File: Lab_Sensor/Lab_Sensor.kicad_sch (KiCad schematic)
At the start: 31 parts, among them U1 ESP32-POE, U2 AM2302, U3 SSD1306, U4 INMP441

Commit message: switched pin 5 and 36
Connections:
- net at D6.A: now also R12.1
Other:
- moved on the sheet: D6
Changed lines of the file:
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@@
 	(wire
 		(pts
+			(xy 153.67 57.15) (xy 210.82 57.15)
+		)
+		(stroke
+			(width 0)
+			(type default)
+		)
+	)
+	(wire
+		(pts
 			(xy 87.63 62.23) (xy 90.17 62.23)
 		)
@@
 	(wire
 		(pts
-			(xy 59.69 90.17) (xy 59.69 92.71)
+			(xy 210.82 90.17) (xy 210.82 92.71)
 		)
 		(stroke
@@
 	(wire
 		(pts
+			(xy 210.82 57.15) (xy 210.82 82.55)
+		)
+		(stroke
+			(width 0)
+			(type default)
+		)
+	)
+	(wire
+		(pts
 			(xy 85.09 74.93) (xy 72.39 74.93)
 		)
@@
 	(symbol
 		(lib_id "Device:LED")
-		(at 59.69 86.36 90)
+		(at 210.82 86.36 90)
 		(unit 1)
 		(exclude_from_sim no)
@@
 		(dnp no)
 		(property "Reference" "D6"
-			(at 60.96 85.598 90)
+			(at 212.09 85.598 90)
 			(effects
 				(font
@@
 		)
 		(property "Value" "LED"
-			(at 60.96 87.63 90)
+			(at 212.09 87.63 90)
 			(effects
 				(font
@@
 		)
 		(property "Footprint" "Custom_Parts:Standard_LED_Throughhole"
-			(at 59.69 86.36 0)
+			(at 210.82 86.36 0)
 			(effects
 				(font
@@
 		)
 		(property "Datasheet" "~"
-			(at 59.69 86.36 0)
+			(at 210.82 86.36 0)
 			(effects
 				(font
@@
 		)
 		(property "Description" "Light emitting diode"
-			(at 59.69 86.36 0)
+			(at 210.82 86.36 0)
 			(effects
 				(font
@@
 		)
 		(property "Sim.Pins" "1=K 2=A"
-			(at 59.69 86.36 0)
+			(at 210.82 86.36 0)
 			(effects
 				(font
@@
 	(symbol
 		(lib_id "power:GND")
-		(at 59.69 92.71 0)
+		(at 210.82 92.71 0)
 		(unit 1)
 		(exclude_from_sim no)
@@
 		(fields_autoplaced yes)
 		(property "Reference" "#PWR08"
-			(at 59.69 99.06 0)
+			(at 210.82 99.06 0)
 			(effects
 				(font
@@
 		)
 		(property "Value" "GND"
-			(at 59.69 97.79 0)
+			(at 210.82 97.79 0)
 			(effects
 				(font
@@
 		)
 		(property "Footprint" ""
-			(at 59.69 92.71 0)
+			(at 210.82 92.71 0)
 			(effects
 				(font
@@
 		)
 		(property "Datasheet" ""
-			(at 59.69 92.71 0)
+			(at 210.82 92.71 0)
 			(effects
 				(font
@@
 		)
 		(property "Description" "Power symbol creates a global label with name \"GND\" , ground"
-			(at 59.69 92.71 0)
+			(at 210.82 92.71 0)
 			(effects
 				(font

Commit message: Switched pin 4 and 1
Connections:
- net at U1.EXT1_6 (GPIO1): now also TP2.TP; no longer R11.2
- net at U1.EXT1_9 (GPIO4): now also R11.2; no longer TP2.TP
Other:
- moved on the sheet: R11, TP2
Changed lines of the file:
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@@
 	(wire
 		(pts
-			(xy 168.91 59.69) (xy 168.91 106.68)
-		)
-		(stroke
-			(width 0)
-			(type default)
-		)
-	)
-	(wire
-		(pts
 			(xy 153.67 62.23) (xy 166.37 62.23)
 		)
@@
 	(wire
 		(pts
-			(xy 168.91 59.69) (xy 153.67 59.69)
+			(xy 168.91 67.31) (xy 153.67 67.31)
 		)
 		(stroke
@@
 	(wire
 		(pts
+			(xy 168.91 106.68) (xy 168.91 67.31)
+		)
+		(stroke
+			(width 0)
+			(type default)
+		)
+	)
+	(wire
+		(pts
 			(xy 130.81 123.19) (xy 130.81 120.65)
 		)
@@
 	(symbol
 		(lib_id "Custom_Parts:5002")
-		(at 153.67 67.31 0)
+		(at 153.67 59.69 0)
 		(unit 1)
 		(exclude_from_sim no)
@@
 		(dnp no)
 		(property "Reference" "TP2"
-			(at 151.638 66.802 0)
+			(at 151.638 59.182 0)
 			(effects
 				(font
@@
 		)
 		(property "Value" "5002"
-			(at 156.21 67.31 0)
+			(at 156.21 59.69 0)
 			(effects
 				(font
@@
 		)
 		(property "Footprint" "Custom_Parts:5002"
-			(at 153.67 67.31 0)
+			(at 153.67 59.69 0)
 			(effects
 				(font
@@
 		)
 		(property "Datasheet" ""
-			(at 153.67 67.31 0)
+			(at 153.67 59.69 0)
 			(effects
 				(font
@@
 		)
 		(property "Description" "TestPoint"
-			(at 153.67 67.31 0)
+			(at 153.67 59.69 0)
 			(effects
 				(font
@@
 		)
 		(property "PARTREV" "H"
-			(at 153.67 67.31 0)
+			(at 153.67 59.69 0)
 			(effects
 				(font
@@
 		)
 		(property "STANDARD" "Manufacturer Recommendations"
-			(at 153.67 67.31 0)
+			(at 153.67 59.69 0)
 			(effects
 				(font
@@
 		)
 		(property "SNAPEDA_PN" "5000"
-			(at 153.67 67.31 0)
+			(at 153.67 59.69 0)
 			(effects
 				(font
@@
 		)
 		(property "MAXIMUM_PACKAGE_HEIGHT" "4.57 mm"
-			(at 153.67 67.31 0)
+			(at 153.67 59.69 0)
 			(effects
 				(font
@@
 		)
 		(property "MANUFACTURER" "Keystone"
-			(at 153.67 67.31 0)
+			(at 153.67 59.69 0)
 			(effects
 				(font
@@
 	(symbol
 		(lib_id "Device:R_Small_US")
-		(at 151.13 59.69 0)
+		(at 151.13 67.31 0)
 		(unit 1)
 		(exclude_from_sim no)
@@
 		(dnp no)
 		(property "Reference" "R11"
-			(at 153.162 58.928 0)
+			(at 153.162 66.548 0)
 			(effects
 				(font
@@
 		)
 		(property "Value" "0R"
-			(at 155.448 58.928 0)
+			(at 155.448 66.548 0)
 			(effects
 				(font
@@
 		)
 		(property "Footprint" "Resistor_SMD:R_0603_1608Metric"
-			(at 151.13 59.69 0)
+			(at 151.13 67.31 0)
 			(effects
 				(font
@@
 		)
 		(property "Datasheet" "~"
-			(at 151.13 59.69 0)
+			(at 151.13 67.31 0)
 			(effects
 				(font
@@
 		)
 		(property "Description" "Resistor, small US symbol"
-			(at 151.13 59.436 0)
+			(at 151.13 67.056 0)
 			(effects
 				(font

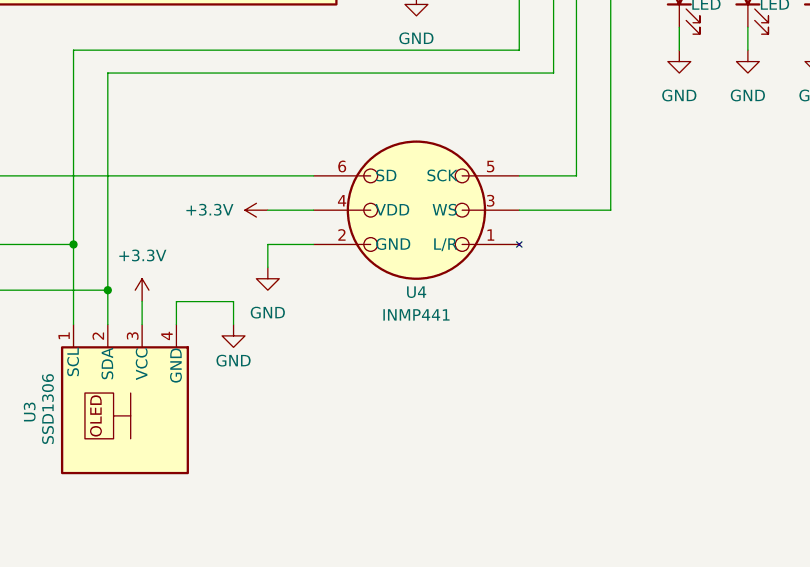
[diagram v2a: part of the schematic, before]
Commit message: Grounded L/R
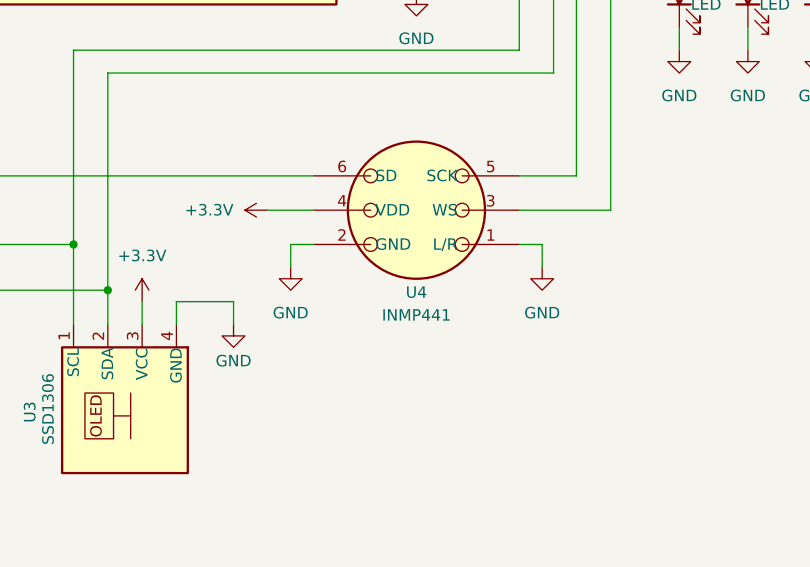
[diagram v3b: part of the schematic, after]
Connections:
- net GND: now also U4.1 (L/R)
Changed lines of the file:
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@@
 	(wire
 		(pts
-			(xy 134.62 114.3) (xy 134.62 116.84)
+			(xy 137.16 114.3) (xy 137.16 116.84)
 		)
 		(stroke
@@
 	(wire
 		(pts
+			(xy 165.1 114.3) (xy 165.1 116.84)
+		)
+		(stroke
+			(width 0)
+			(type default)
+		)
+	)
+	(wire
+		(pts
 			(xy 74.93 125.73) (xy 74.93 127)
 		)
@@
 	(wire
 		(pts
-			(xy 139.7 114.3) (xy 134.62 114.3)
+			(xy 139.7 114.3) (xy 137.16 114.3)
 		)
 		(stroke
@@
 	(wire
 		(pts
+			(xy 162.56 114.3) (xy 165.1 114.3)
+		)
+		(stroke
+			(width 0)
+			(type default)
+		)
+	)
+	(wire
+		(pts
 			(xy 54.61 111.76) (xy 54.61 114.3)
 		)
@@
 	)
 	(symbol
+		(lib_id "power:GND")
+		(at 165.1 116.84 0)
+		(unit 1)
+		(exclude_from_sim no)
+		(in_bom yes)
+		(on_board yes)
+		(dnp no)
+		(fields_autoplaced yes)
+		(property "Reference" "#PWR017"
+			(at 165.1 123.19 0)
+			(effects
+				(font
+					(size 1.27 1.27)
+				)
+				(hide yes)
+			)
+		)
+		(property "Value" "GND"
+			(at 165.1 121.92 0)
+			(effects
+				(font
+					(size 1.27 1.27)
+				)
+			)
+		)
+		(property "Footprint" ""
+			(at 165.1 116.84 0)
+			(effects
+				(font
+					(size 1.27 1.27)
+				)
+				(hide yes)
+			)
+		)
+		(property "Datasheet" ""
+			(at 165.1 116.84 0)
+			(effects
+				(font
+					(size 1.27 1.27)
+				)
+				(hide yes)
+			)
+		)
+		(property "Description" "Power symbol creates a global label with name \"GND\" , ground"
+			(at 165.1 116.84 0)
+			(effects
+				(font
+					(size 1.27 1.27)
+				)
+				(hide yes)
+			)
+		)
+		(pin "1"
+		)
+		(instances
+			(project ""
+				(path "/37cc0d69-8e3e-4377-b528-04310444116a"
+					(reference "#PWR017")
+					(unit 1)
+				)
+			)
+		)
+	)
+	(symbol
 		(lib_id "Mechanical:MountingHole")
 		(at 58.42 184.15 0)
@@
 	(symbol
 		(lib_id "power:GND")
-		(at 134.62 116.84 0)
+		(at 137.16 116.84 0)
 		(mirror y)
 		(unit 1)
@@
 		(fields_autoplaced yes)
 		(property "Reference" "#PWR015"
-			(at 134.62 123.19 0)
+			(at 137.16 123.19 0)
 			(effects
 				(font
@@
 		)
 		(property "Value" "GND"
-			(at 134.62 121.92 0)
+			(at 137.16 121.92 0)
 			(effects
 				(font
@@
 		)
 		(property "Footprint" ""
-			(at 134.62 116.84 0)
+			(at 137.16 116.84 0)
 			(effects
 				(font
@@
 		)
 		(property "Datasheet" ""
-			(at 134.62 116.84 0)
+			(at 137.16 116.84 0)
 			(effects
 				(font
@@
 		)
 		(property "Description" "Power symbol creates a global label with name \"GND\" , ground"
-			(at 134.62 116.84 0)
+			(at 137.16 116.84 0)
 			(effects
 				(font
